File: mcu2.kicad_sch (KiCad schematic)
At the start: 54 parts, among them J67 Conn_01x22, J68 Conn_01x22, J69 Conn_01x22, J70 Conn_01x22, J71 Conn_01x22, J72 Conn_01x22, J73 Conn_01x22, J74 Conn_01x22, J75 Conn_01x22, J76 Conn_01x22

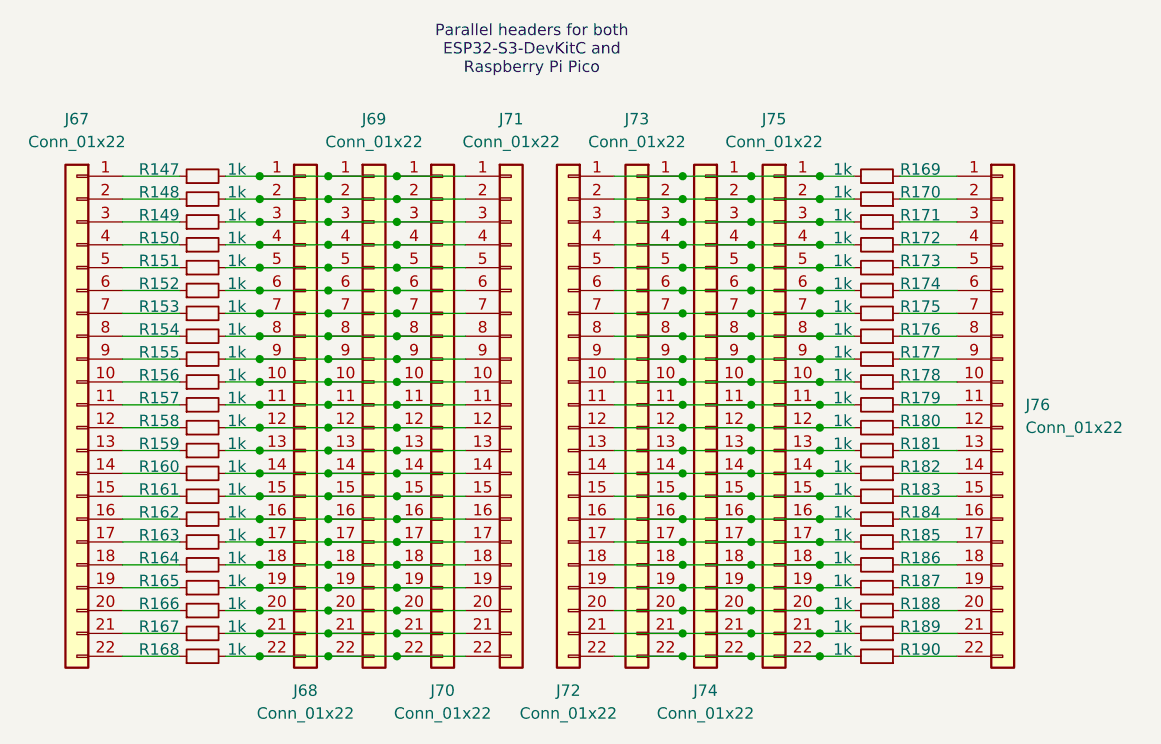
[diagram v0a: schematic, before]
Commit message: Assign part numbers and finish other 0.2.0 changes
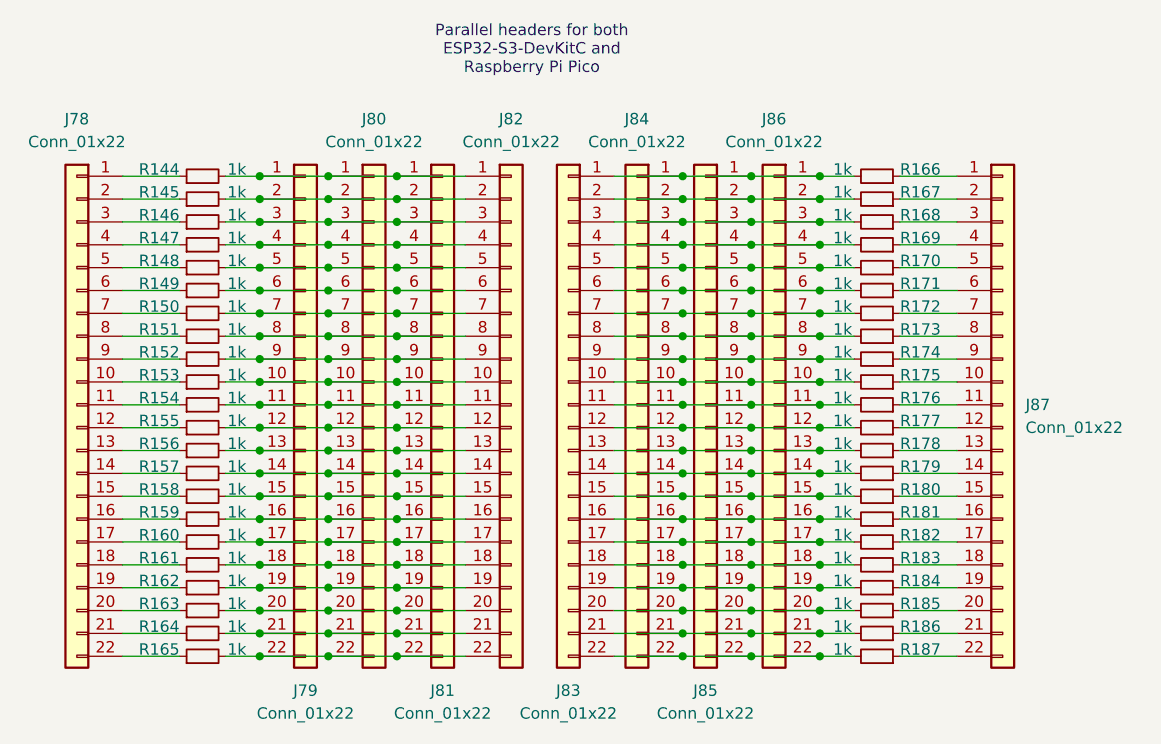
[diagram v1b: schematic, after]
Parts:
- renumbered J67 to J78, J68 to J79, J69 to J80, J70 to J81, J71 to J82, J72 to J83, J73 to J84, J74 to J85, J75 to J86, J76 to J87, R147 to R144, R148 to R145, R149 to R146, R150 to R147, R151 to R148, R152 to R149, R153 to R150, R154 to R151, R155 to R152, R156 to R153, R157 to R154, R158 to R155, R159 to R156, R160 to R157, R161 to R158, R162 to R159, R163 to R160, R164 to R161, R165 to R162, R166 to R163, R167 to R164, R168 to R165, R169 to R166, R170 to R167, R171 to R168, R172 to R169, R173 to R170, R174 to R171, R175 to R172, R176 to R173, R177 to R174, R178 to R175, R179 to R176, R180 to R177, R181 to R178, R182 to R179, R183 to R180, R184 to R181, R185 to R182, R186 to R183, R187 to R184, R188 to R185, R189 to R186, R190 to R187

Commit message: Update the title blocks
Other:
- company: (none) -> Hat Labs Oy
- title: (none) -> HALSPA - Hat Labs Spaghetti Board
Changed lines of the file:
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@@
 	(generator_version "9.0")
 	(paper "A4")
+	(title_block
+		(title "HALSPA - Hat Labs Spaghetti Board")
+		(date "2025-04-17")
+		(rev "v0.2.0")
+		(company "Hat Labs Oy")
+		(comment 1 "See the accompanying LICENSE.md file for license details.")
+	)
 	(text "Parallel headers for both\nESP32-S3-DevKitC and\nRaspberry Pi Pico"
 		(exclude_from_sim no)

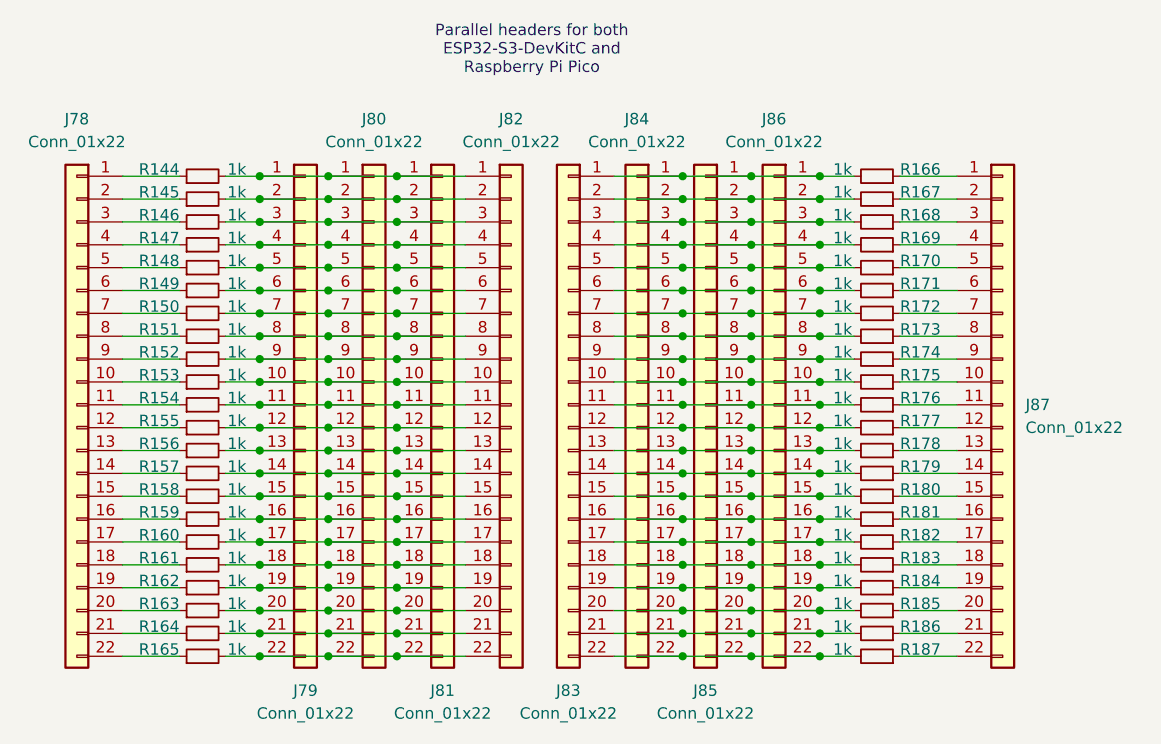
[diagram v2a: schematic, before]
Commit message: Improve MCU2 layout; document curlim12v CSA
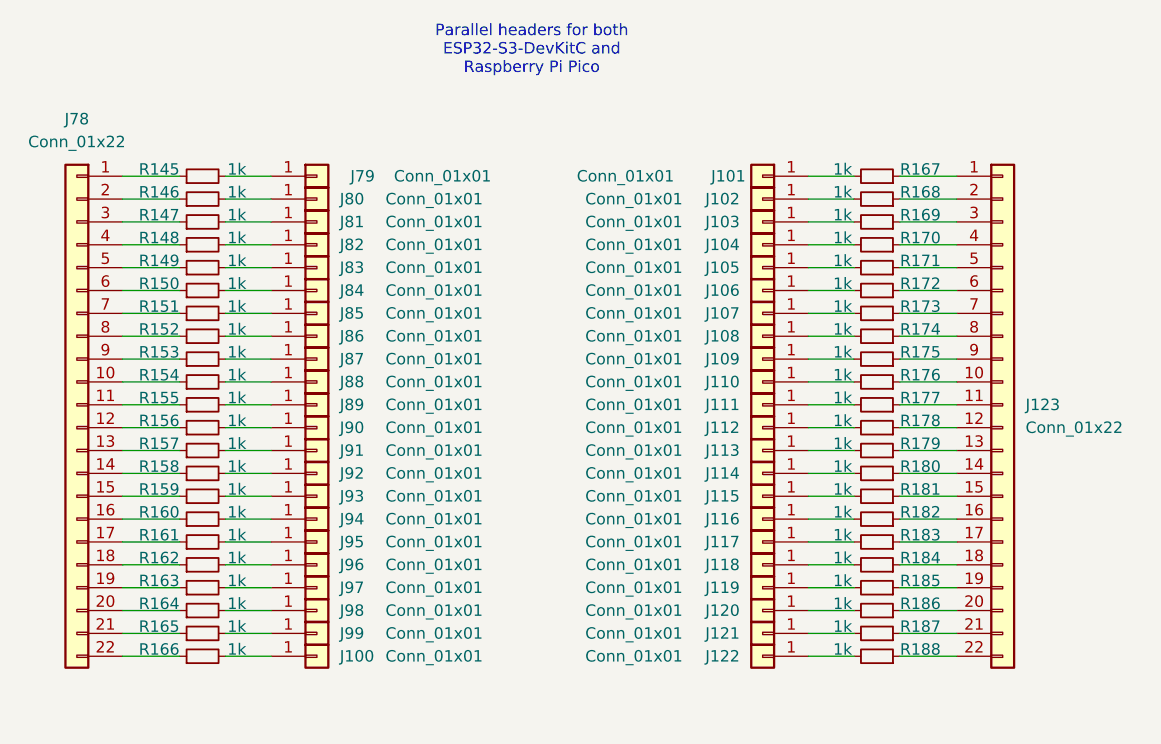
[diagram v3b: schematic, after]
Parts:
- removed J79, J80, J81, J82, J83, J84, J85, J86: Conn_01x22, HL_Connector_Pad_2.54mm:Pad_1x22_P2.54_1.7x1.7_Oct, symbol Connector_Generic:Conn_01x22
- added J100, J101, J102, J103, J104, J105, J106, J107, J108, J109, J110, J111, J112, J113, J114, J115, J116, J117, J118, J119, J120, J121, J122, J79, J80, J81, J82, J83, J84, J85, J86, J87, J88, J89, J90, J91, J92, J93, J94, J95, J96, J97, J98, J99: Conn_01x01, HL_Connector_Pad_2.54mm:Pad_1x04_P2.54_1.7x1.7_Oct_Connected, symbol Connector_Generic:Conn_01x01
- renumbered J87 to J123, R144 to R145, R145 to R146, R146 to R147, R147 to R148, R148 to R149, R149 to R150, R150 to R151, R151 to R152, R152 to R153, R153 to R154, R154 to R155, R155 to R156, R156 to R157, R157 to R158, R158 to R159, R159 to R160, R160 to R161, R161 to R162, R162 to R163, R163 to R164, R164 to R165, R165 to R166, R166 to R167, R167 to R168, R168 to R169, R169 to R170, R170 to R171, R171 to R172, R172 to R173, R173 to R174, R174 to R175, R175 to R176, R176 to R177, R177 to R178, R178 to R179, R179 to R180, R180 to R181, R181 to R182, R182 to R183, R183 to R184, R184 to R185, R185 to R186, R186 to R187, R187 to R188
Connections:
- net at R155.2: now also J89.1 (Pin_1)
- net at R175.2: now also J109.1 (Pin_1)
- net at R166.2: now also J100.1 (Pin_1)
- net at R145.2: now also J79.1 (Pin_1)
- net at R154.2: now also J88.1 (Pin_1)
- net at R156.2: now also J90.1 (Pin_1)
- net at R157.2: now also J91.1 (Pin_1)
- net at R158.2: now also J92.1 (Pin_1)
- net at R159.2: now also J93.1 (Pin_1)
- net at R160.2: now also J94.1 (Pin_1)
- net at R161.2: now also J95.1 (Pin_1)
- net at R162.2: now also J96.1 (Pin_1)
- net at R163.2: now also J97.1 (Pin_1)
- net at R146.2: now also J80.1 (Pin_1)
- net at R164.2: now also J98.1 (Pin_1)
- net at R165.2: now also J99.1 (Pin_1)
- net at R147.2: now also J81.1 (Pin_1)
- net at R148.2: now also J82.1 (Pin_1)
- net at R149.2: now also J83.1 (Pin_1)
- net at R150.2: now also J84.1 (Pin_1)
- net at R151.2: now also J85.1 (Pin_1)
- net at R152.2: now also J86.1 (Pin_1)
- net at R153.2: now also J87.1 (Pin_1)
- net at R167.2: now also J101.1 (Pin_1)
- net at R176.2: now also J110.1 (Pin_1)
- net at R177.2: now also J111.1 (Pin_1)
- net at R178.2: now also J112.1 (Pin_1)
- net at R179.2: now also J113.1 (Pin_1)
- net at R180.2: now also J114.1 (Pin_1)
- net at R181.2: now also J115.1 (Pin_1)
- net at R182.2: now also J116.1 (Pin_1)
- net at R183.2: now also J117.1 (Pin_1)
- net at R184.2: now also J118.1 (Pin_1)
- net at R185.2: now also J119.1 (Pin_1)
- net at R168.2: now also J102.1 (Pin_1)
- net at R186.2: now also J120.1 (Pin_1)
- net at R187.2: now also J121.1 (Pin_1)
- net at R188.2: now also J122.1 (Pin_1)
- net at R169.2: now also J103.1 (Pin_1)
- net at R170.2: now also J104.1 (Pin_1)
- net at R171.2: now also J105.1 (Pin_1)
- net at R172.2: now also J106.1 (Pin_1)
- net at R173.2: now also J107.1 (Pin_1)
- net at R174.2: now also J108.1 (Pin_1)

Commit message: Assorted fixes
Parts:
- renumbered J106 to J1106, J107 to J1107
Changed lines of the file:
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@@
 		(on_board yes)
 		(dnp no)
-		(property "Reference" "J106"
+		(property "Reference" "J1106"
 			(at 166.37 78.74 0)
 			(effects
@@
 			(project "HALSPA"
 				(path "/7eeba806-440e-4671-bc07-69fe183910a7/0857553c-a85e-4345-93e2-1af8db70e954"
-					(reference "J106")
+					(reference "J1106")
 					(unit 1)
 				)
@@
 		(on_board yes)
 		(dnp no)
-		(property "Reference" "J107"
+		(property "Reference" "J1107"
 			(at 166.37 81.28 0)
 			(effects
@@
 			(project "HALSPA"
 				(path "/7eeba806-440e-4671-bc07-69fe183910a7/0857553c-a85e-4345-93e2-1af8db70e954"
-					(reference "J107")
-					(unit 1)
-				)
+					(reference "J1107")
+					(unit 1)
+				)
